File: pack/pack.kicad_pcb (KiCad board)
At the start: 2 copper layers, 48 x 28.1 mm, 8 parts

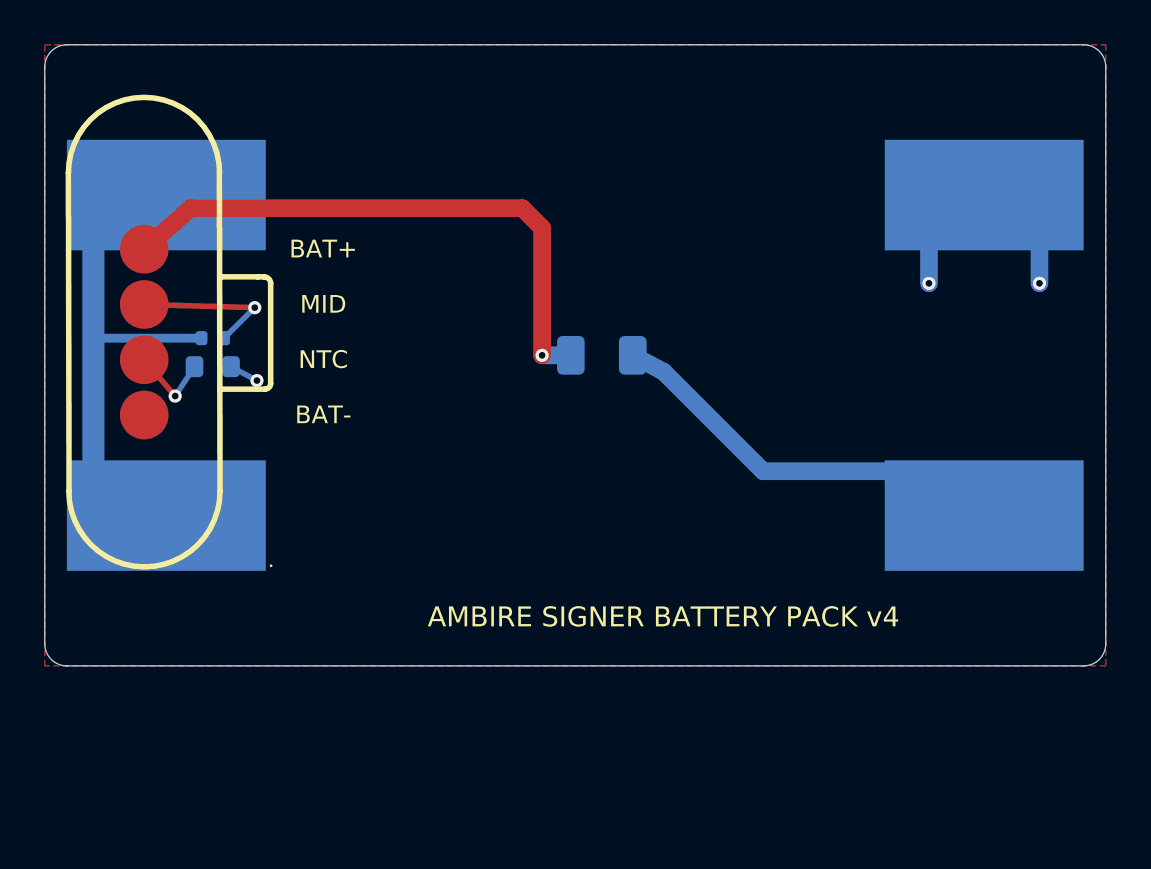
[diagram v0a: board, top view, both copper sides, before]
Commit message: Pack board: the through-hole magnetic male (C5126845), no loose magnets, 0.6 mm south
The pack's connector is now Xinyangze's magnetic male YZP0048-20048-04025-03, mating
with the device's receptacle. Its land is ours from the maker's drawing (0.80 mm holes,
1.60 mm pads; EasyEDA's has a 0.05 mm ring), with our model. The outline and the cells
come from docs/v4/enclosure/enclosure.json now (0.57 mm south); the magnet rings are gone.

The pin column sits at x 36.5, not the case's 43.6: there it lands on the east clips'
steel bases (BAT- on the south clip's CELL+ pad) and its joints would sit under the
clips' arms; makePack.py refuses any position on a base. The fuse, resistor and
thermistor sit on their pins' lines. DRC: nothing at any severity, as saved and refilled;
cleanCopper --check clean. Order set regenerated: SMT bottom + THT for the connector.

Co-Authored-By: Claude Opus 5.5 <noreply@anthropic.com>
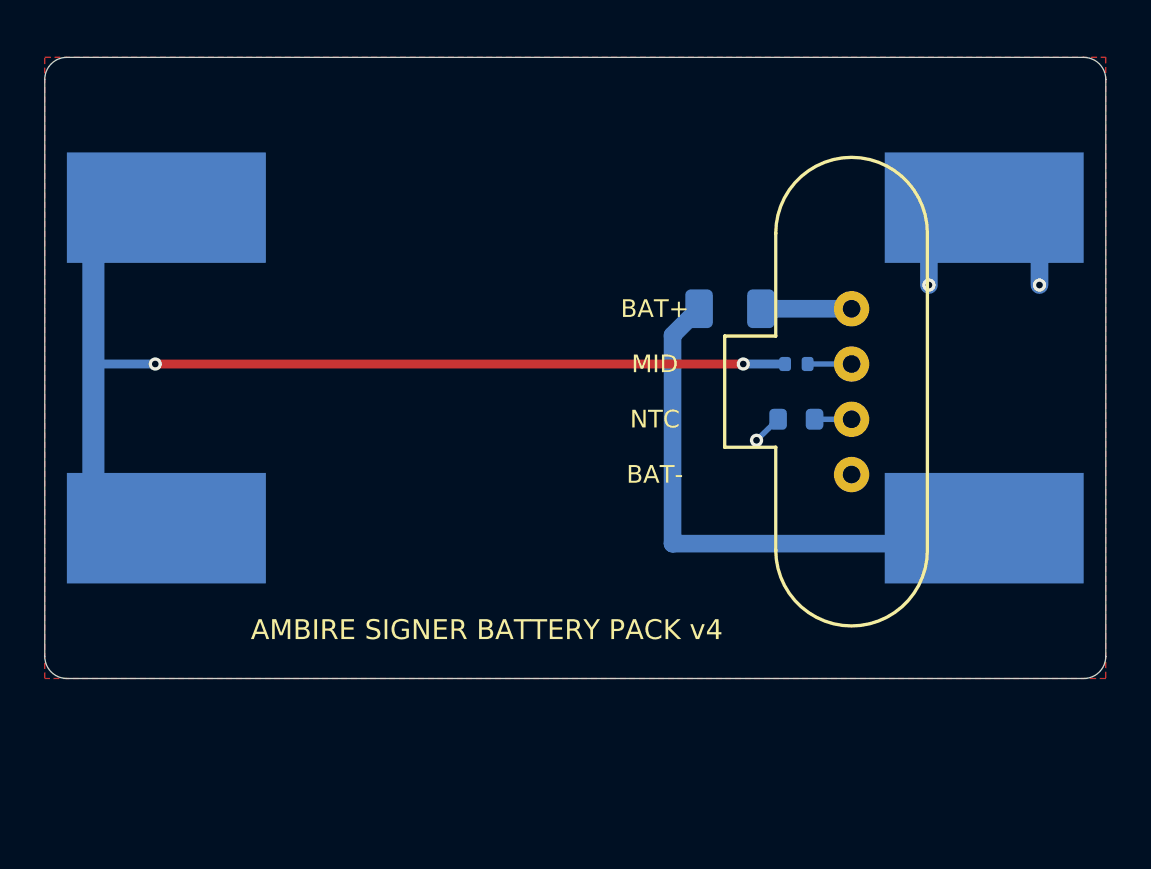
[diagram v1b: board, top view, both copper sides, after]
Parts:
- removed the J_PACK at (4.50, 32.7)
- added J_PACK: YZP0048-20048-04025-03, Xinyangze_YZP0048-20048-04025-03, F.Cu at (36.5, 35.4)
- moved RT_PACK 26.5 mm to (34.0, 36.6)
- moved R_MID 26.4 mm to (34.0, 34.1)
- moved F_BAT 6.17 mm to (31.0, 31.6)
- moved BT_N1 0.57 mm to (42.5, 27.1)
- moved BT_N2 0.57 mm to (5.50, 41.6)
- moved BT_P1 0.57 mm to (5.50, 27.1)
- moved BT_P2 0.57 mm to (42.5, 41.6)
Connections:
- F_BAT pad 1: BAT+ -> CELL+
- F_BAT pad 2: CELL+ -> BAT+
- RT_PACK pad 1: NTC -> BAT-
- RT_PACK pad 2: BAT- -> NTC
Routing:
- net MID: track 15.4 -> 41.8 mm, vias 0 -> 2
- net BAT+: track 26.1 -> 4.10 mm, vias 1 -> 0
- net CELL+: track 14.0 -> 21.3 mm
- net MID_SENSE: track 6.96 -> 1.99 mm, vias 1 -> 0
- net NTC: track 3.75 -> 1.67 mm, vias 1 -> 0
- net BAT-: track 5.33 -> 4.36 mm
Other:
- board text removed: "MAGNET"

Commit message: Pack board: Ambire Ice on its silkscreen and title block
Co-Authored-By: Claude Opus 5.5 <noreply@anthropic.com>
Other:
- board text added: "AMBIRE ICE BATTERY PACK v4"
- board text removed: "AMBIRE SIGNER BATTERY PACK v4"

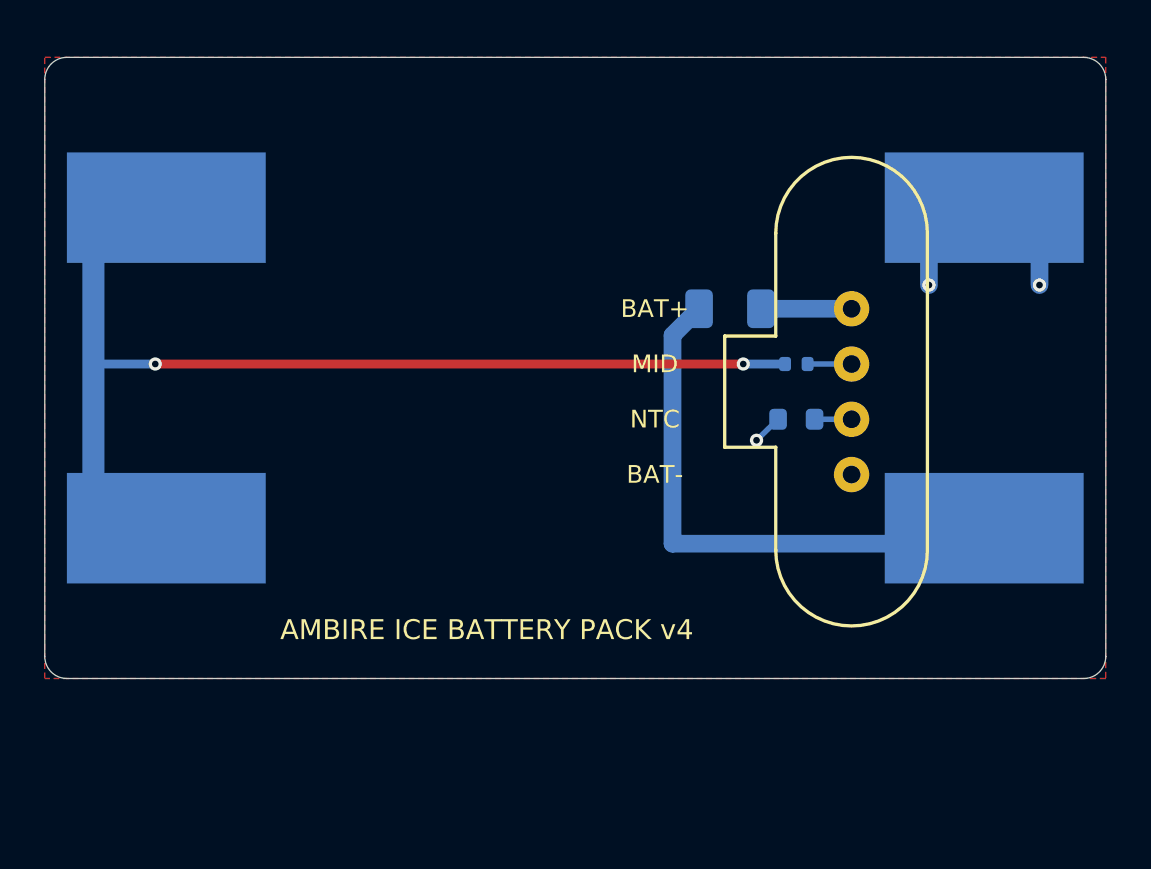
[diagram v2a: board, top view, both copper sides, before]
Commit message: Pack board: the male back over the receptacle (43.6, 37.6), its joints between the spread cells' clips
The case spreads the cells 21.1 mm apart (y 27.077 and 48.177) so the magnetic male's
through-hole joints pass between the east clips' arms: 0.50 mm from each arm, checked by
makePack.py (it now reads the connector's place from enclosure.json and refuses a joint
within 0.4 mm of an arm or 0.2 mm of a base). The fuse (34.5, 33.877), the 1 k resistor
(36.0, 36.377) and the thermistor (36.0, 38.877) sit on their pins' lines, west of the
clips' arms; CELL+ runs round them to the south-east clip. DRC: nothing at any severity,
as saved and refilled; cleanCopper --check clean; order set regenerated.

Co-Authored-By: Claude Opus 5.5 <noreply@anthropic.com>
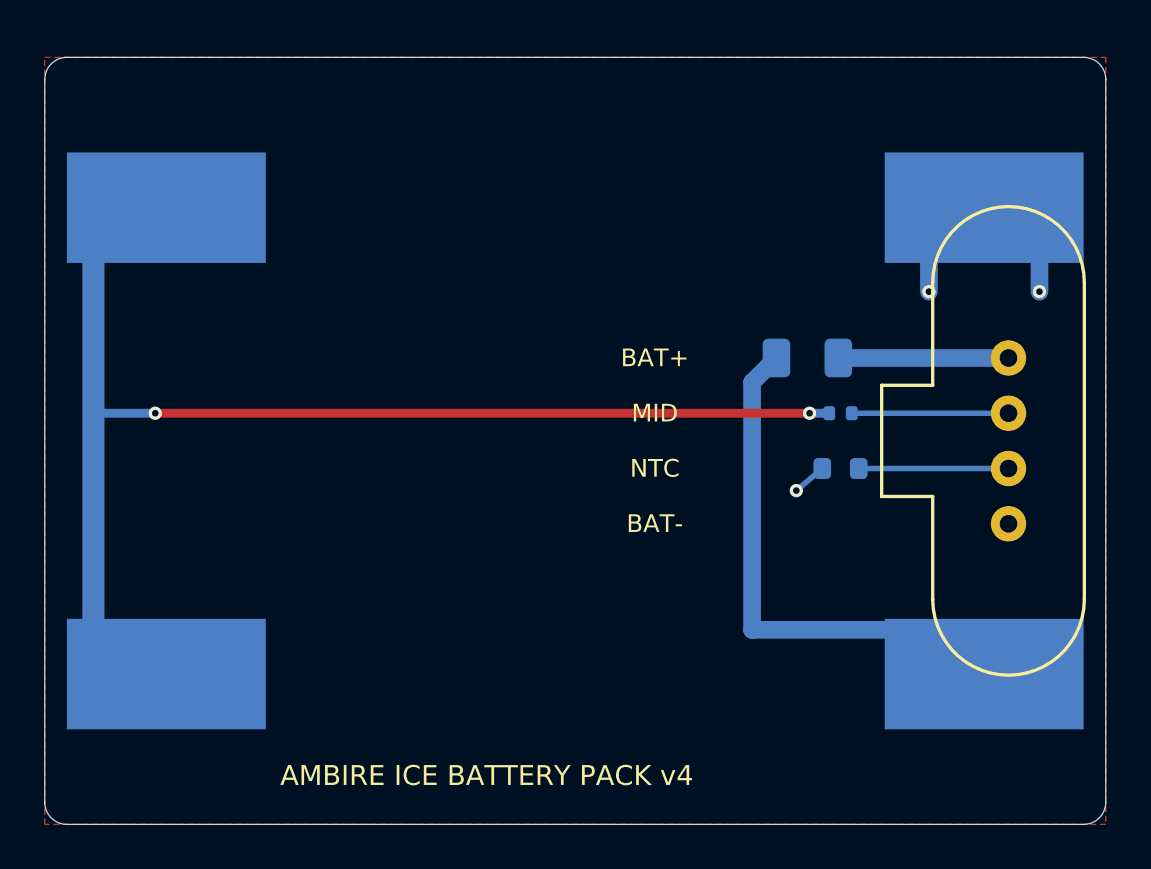
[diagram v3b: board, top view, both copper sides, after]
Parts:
- moved J_PACK 7.44 mm to (43.6, 37.6)
- moved BT_N2 6.60 mm to (5.50, 48.2)
- moved BT_P2 6.60 mm to (42.5, 48.2)
- moved F_BAT 4.15 mm to (34.5, 33.9)
- moved RT_PACK 2.99 mm to (36.0, 38.9)
- moved R_MID 2.99 mm to (36.0, 36.4)
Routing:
- net MID: track 41.8 -> 50.4 mm
- net NTC: track 1.67 -> 6.77 mm
- net MID_SENSE: track 1.99 -> 7.09 mm
- net BAT+: track 4.10 -> 7.70 mm
- net CELL+: track 21.3 -> 19.4 mm
- net BAT-: track 4.36 -> 5.14 mm
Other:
- board size 48 x 28.1 mm -> 48 x 34.7 mm

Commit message: v4 pack: the cells 16.7 mm apart, not 21.1: the joints clear the clips' steel bases, not their arms' span
The cell pitch kept the magnetic male's four joints 0.5 mm outside the clips' arms, as if
the arms lay on the board. Only the steel base (7 mm across the cell) does: the clips'
models show the arms leaving it at its edge and curving up (0.66 mm up 0.3 mm out, 1.36
mm 0.9 mm out). The case now derives the pitch from the bases plus 0.3 mm: 16.7 mm, the
cans 6.2 mm apart (were 10.6). The pack is 51.2 x 33.1 mm (was 37.5), its board 48.0 x
30.3; the receptacle on the device moves 2.2 mm north to (43.6, 35.43), the same parts
to move off its land as before.

Pack board rebuilt by makePack.py: it checks the joints 0.3 mm off every base; the north
cell's two minus vias move north of its clip (the BAT+ pin now sits where they were);
KiCad's PTH-in-courtyard check is off on this board (the clips' courtyards are the arms'
span, J_PACK its only through-hole part). DRC: nothing, as saved and refilled;
cleanCopper --check clean; order set and renders regenerated. The outer two joints now
sit partly under the arms (1.65 mm up over their centres): soldered with a tilted iron.

Also the v4 page footer's leftover "Ambire Signer" -> "Ambire Ice".

Co-Authored-By: Claude Opus 5.5 <noreply@anthropic.com>
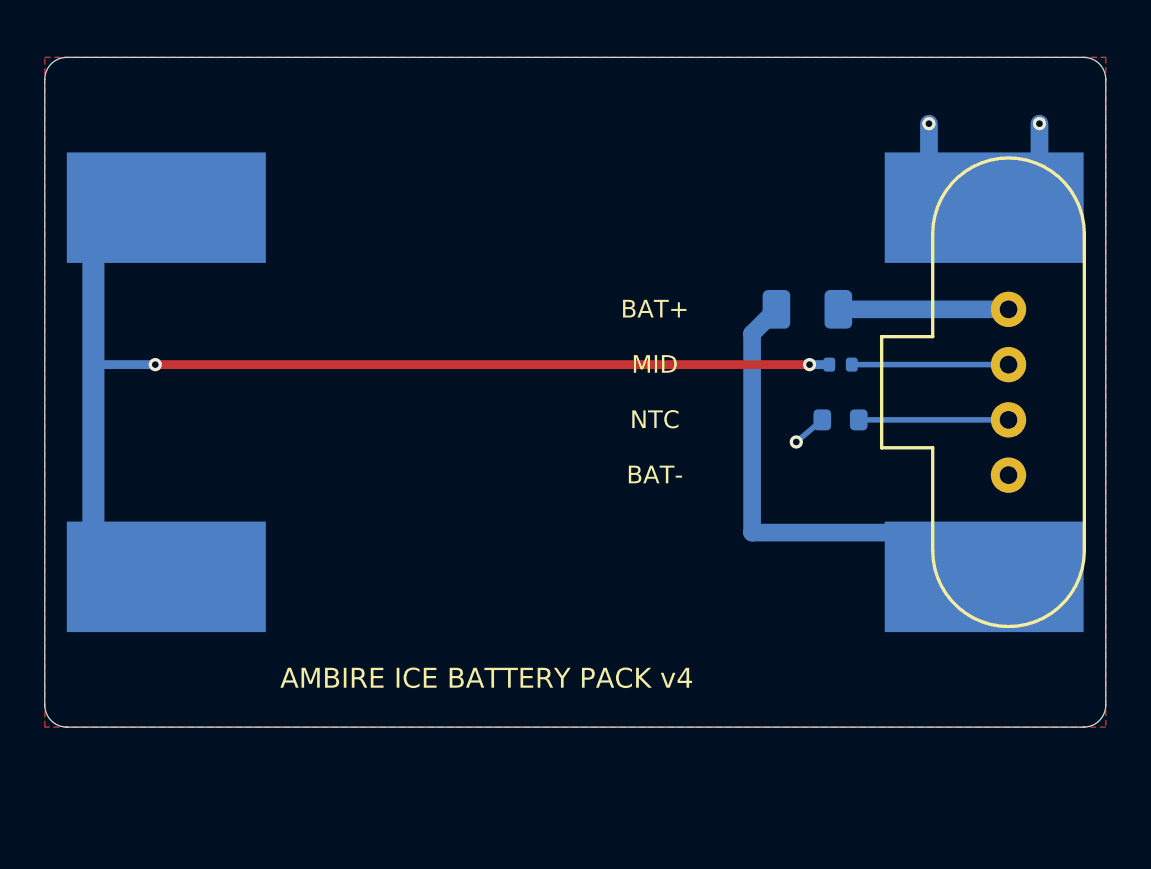
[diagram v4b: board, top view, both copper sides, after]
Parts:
- moved BT_N2 4.40 mm to (5.50, 43.8)
- moved BT_P2 4.40 mm to (42.5, 43.8)
- moved F_BAT 2.20 mm to (34.5, 31.7)
- moved J_PACK 2.20 mm to (43.6, 35.4)
- moved RT_PACK 2.20 mm to (36.0, 36.7)
- moved R_MID 2.20 mm to (36.0, 34.2)
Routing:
- net MID: track 50.4 -> 46.0 mm
- net CELL+: track 19.4 -> 17.2 mm
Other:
- board size 48 x 34.7 mm -> 48 x 30.3 mm

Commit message: v4 pack: the cells 14.6 mm apart: the joints clear the clips' real feet, beside their tabs
The last pitch (16.7 mm) still kept the magnetic male's joints off a 10 x 7 mm block per
clip. The clips' models show each foot is a cross: a body 5 mm across the cell along the
clip (its 9 x 5 pad), and a tab 7 mm across but only 4 mm along it (x 38.5-42.5 on both
east clips), from which the arms rise; nothing else of the clip comes near the board.
The pins stand at x 43.6, just east of the tabs, so only the bodies limit them.

enclosure/generate.py now reads that steel from the clips' placed models (pack_steel,
within 0.5 mm of the pack board; exported as pack.clipSteel) and spaces the cells so the
pins' pads keep 0.3 mm off it (pin_reach): 14.6 mm, the cans 4.1 mm apart. The pads go
1.6 -> 1.5 mm so they clear the tabs' ends by 0.33. The pack can no longer keep its
north edge at the camera's cone: the receptacle would land on J_CTP; it now slides south
until the receptacle clears every part the board cannot move (0.25 mm). Pack 51.2 x 31.0
mm (was 33.1, and 37.5 before), board 48.0 x 28.2, receptacle at (43.6, 34.63), the same
parts to move off its land. A new check keeps each small part 0.3 mm under the cans.

Pack board (makePack.py): joints checked against clipSteel; the fuse turned along the
strip between the cans, the resistor and thermistor on their pins' lines there, west of
the east clips' courtyards; BAT+ runs 0.3 mm outside the north clip's tab, CELL+ to the
south-east clip. DRC: nothing, as saved and refilled; cleanCopper --check clean; no B
copper within 0.30 mm of another net's clip steel. Order set, renders, the v4 page's
model and hero regenerated.

Co-Authored-By: Claude Opus 5.5 <noreply@anthropic.com>
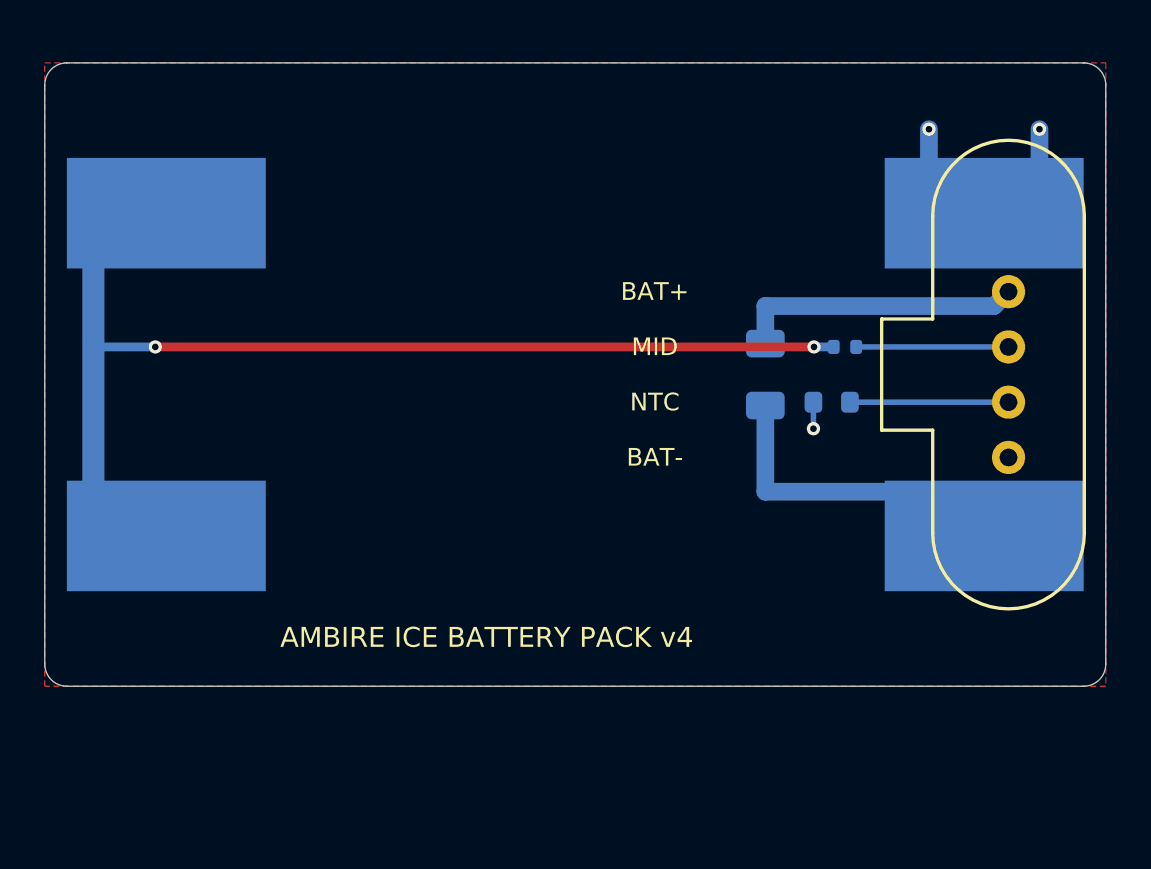
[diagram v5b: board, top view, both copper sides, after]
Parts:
- moved F_BAT 3.51 mm to (32.6, 34.6), turned to 90 degrees
- moved BT_N2 1.85 mm to (5.50, 41.9)
- moved BT_P2 1.85 mm to (42.5, 41.9)
- moved RT_PACK 0.89 mm to (35.6, 35.9)
- moved R_MID 0.82 mm to (36.2, 33.4)
- moved J_PACK 0.80 mm to (43.6, 34.6)
- moved BT_N1 0.25 mm to (42.5, 27.3)
- moved BT_P1 0.25 mm to (5.50, 27.3)
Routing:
- net CELL+: track 17.2 -> 9.90 mm
- net BAT+: track 7.70 -> 13.0 mm
- net MID: track 46.0 -> 44.1 mm
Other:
- board size 48 x 30.3 mm -> 48 x 28.2 mm
